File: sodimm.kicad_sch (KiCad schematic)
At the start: 3 parts, among them J1 PCB-Edge_SODIMM_144_SDR

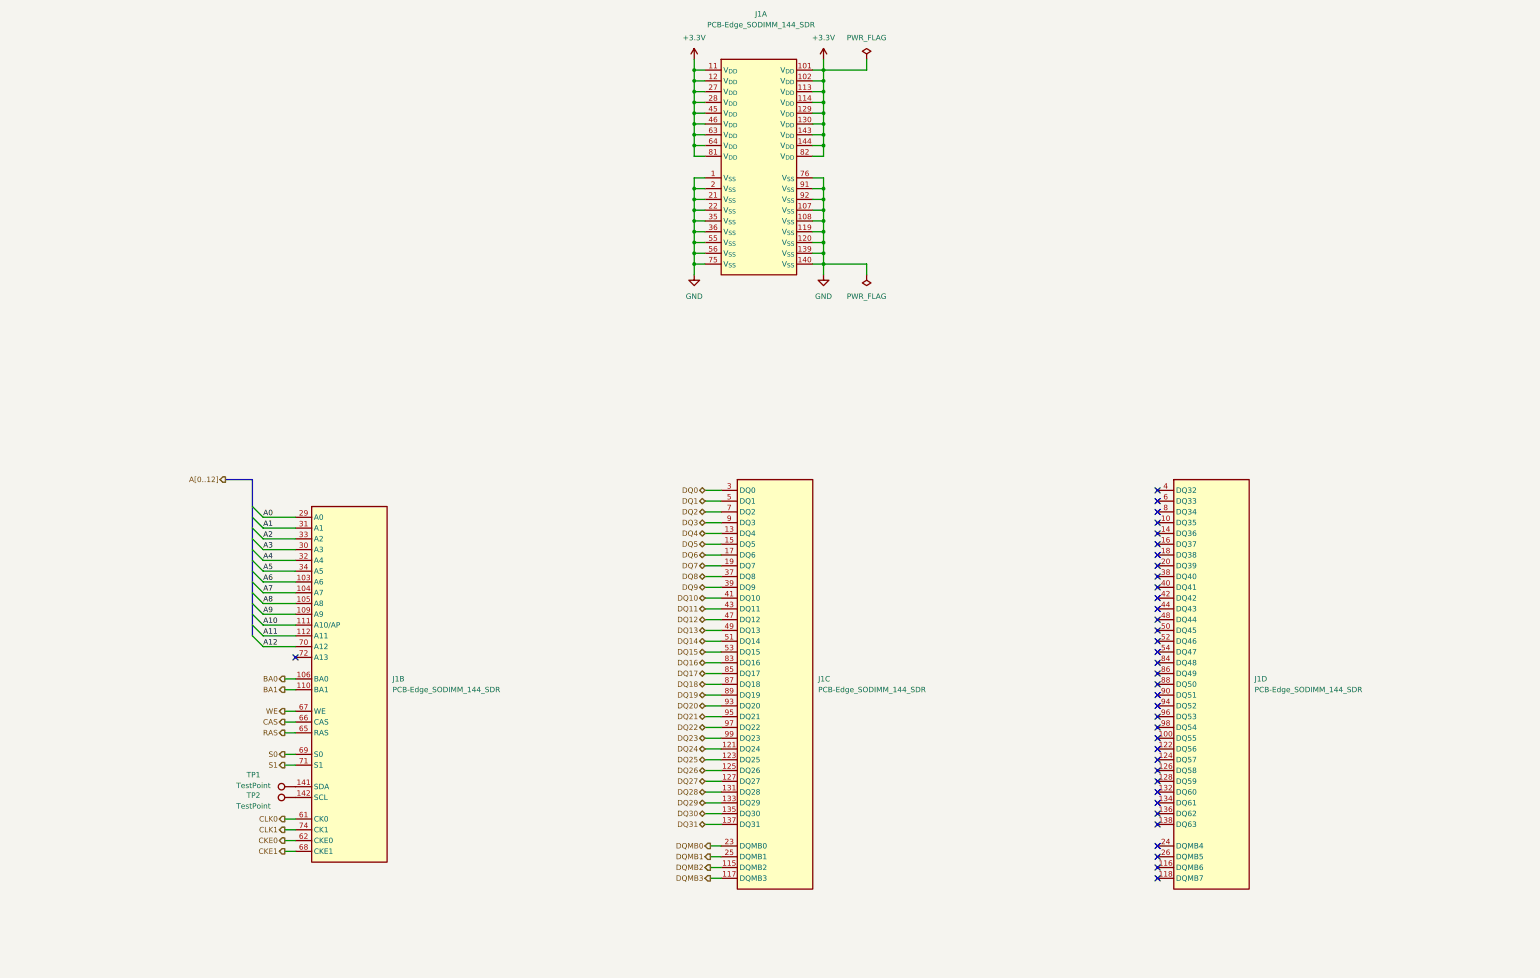
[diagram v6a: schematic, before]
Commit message: [#100470] Change schematic hierarchy
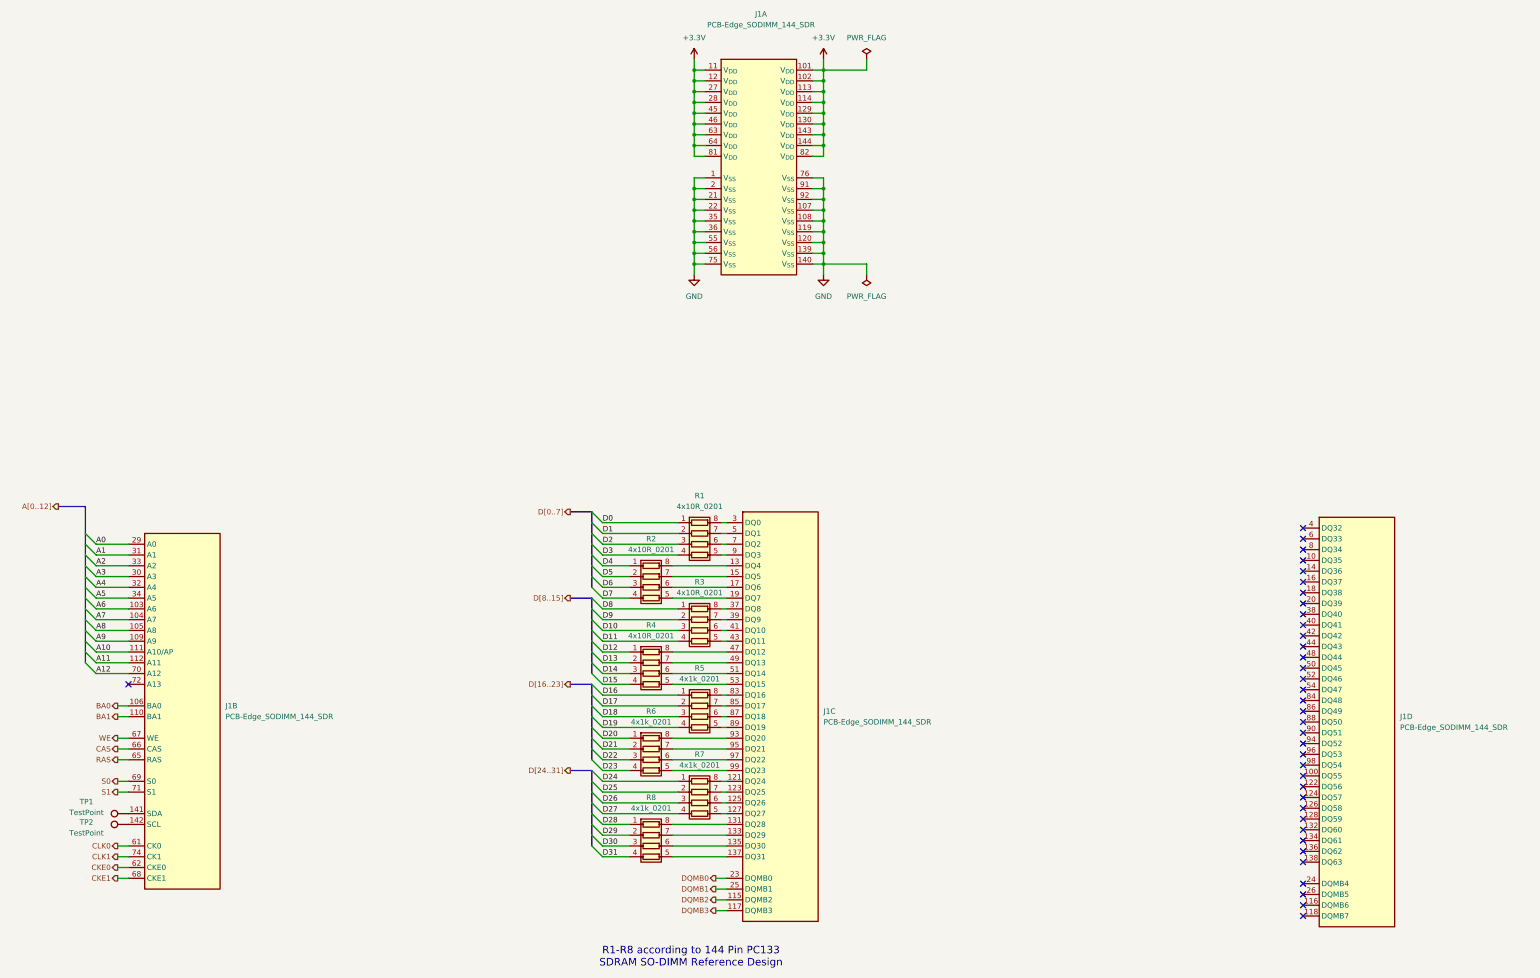
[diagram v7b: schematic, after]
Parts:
- added R1, R2, R3, R4: 4x10R_0201_array, antmicro-footprints:R_Array_4x0201_Panasonic_EXB18V, symbol antmicroResistorNetworksArrays:4x10R_0201_array
- added R5, R6, R7, R8: 4x1k_0201_array, antmicro-footprints:R_Array_4x0201_Panasonic_EXB18V, symbol antmicroResistorNetworksArrays:4x1k_0201_array
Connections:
- net DQ0: no longer names the net of J1.3 (DQ0)
- net DQ0: now also R1.8 (R1.2)
- net DQ1: no longer names the net of J1.5 (DQ1)
- net DQ1: now also R1.7 (R2.2)
- net DQ10: no longer names the net of J1.41 (DQ10)
- net DQ10: now also R3.6 (R3.2)
- net DQ11: no longer names the net of J1.43 (DQ11)
- net DQ11: now also R3.5 (R4.2)
- net DQ12: no longer names the net of J1.47 (DQ12)
- net DQ12: now also R4.8 (R1.2)
- net DQ13: no longer names the net of J1.49 (DQ13)
- net DQ13: now also R4.7 (R2.2)
- net DQ14: no longer names the net of J1.51 (DQ14)
- net DQ14: now also R4.6 (R3.2)
- net DQ15: no longer names the net of J1.53 (DQ15)
- net DQ15: now also R4.5 (R4.2)
- net DQ16: no longer names the net of J1.83 (DQ16)
- net DQ16: now also R5.8 (R1.2)
- net DQ17: no longer names the net of J1.85 (DQ17)
- net DQ17: now also R5.7 (R2.2)
- net DQ18: no longer names the net of J1.87 (DQ18)
- net DQ18: now also R5.6 (R3.2)
- net DQ19: no longer names the net of J1.89 (DQ19)
- net DQ19: now also R5.5 (R4.2)
- net DQ2: no longer names the net of J1.7 (DQ2)
- net DQ2: now also R1.6 (R3.2)
- net DQ20: no longer names the net of J1.93 (DQ20)
- net DQ20: now also R6.8 (R1.2)
- net DQ21: no longer names the net of J1.95 (DQ21)
- net DQ21: now also R6.7 (R2.2)
- net DQ22: no longer names the net of J1.97 (DQ22)
- net DQ22: now also R6.6 (R3.2)
- net DQ23: no longer names the net of J1.99 (DQ23)
- net DQ23: now also R6.5 (R4.2)
- net DQ24: no longer names the net of J1.121 (DQ24)
- net DQ24: now also R7.8 (R1.2)
- net DQ25: no longer names the net of J1.123 (DQ25)
- net DQ25: now also R7.7 (R2.2)
- net DQ26: no longer names the net of J1.125 (DQ26)
- net DQ26: now also R7.6 (R3.2)
- net DQ27: no longer names the net of J1.127 (DQ27)
- net DQ27: now also R7.5 (R4.2)
- net DQ28: no longer names the net of J1.131 (DQ28)
- net DQ28: now also R8.8 (R1.2)
- net DQ29: no longer names the net of J1.133 (DQ29)
- net DQ29: now also R8.7 (R2.2)
- net DQ3: no longer names the net of J1.9 (DQ3)
- net DQ3: now also R1.5 (R4.2)
- net DQ30: no longer names the net of J1.135 (DQ30)
- net DQ30: now also R8.6 (R3.2)
- net DQ31: no longer names the net of J1.137 (DQ31)
- net DQ31: now also R8.5 (R4.2)
- net DQ4: no longer names the net of J1.13 (DQ4)
- net DQ4: now also R2.8 (R1.2)
- net DQ5: no longer names the net of J1.15 (DQ5)
- net DQ5: now also R2.7 (R2.2)
- net DQ6: no longer names the net of J1.17 (DQ6)
- net DQ6: now also R2.6 (R3.2)
- net DQ7: no longer names the net of J1.19 (DQ7)
- net DQ7: now also R2.5 (R4.2)
- net DQ8: no longer names the net of J1.37 (DQ8)
- net DQ8: now also R3.8 (R1.2)
- net DQ9: no longer names the net of J1.39 (DQ9)
- net DQ9: now also R3.7 (R2.2)
- new net D0: R1.1 (R1.1)
- new net D1: R1.2 (R2.1)
- new net D10: R3.3 (R3.1)
- new net D11: R3.4 (R4.1)
- new net D12: R4.1 (R1.1)
- new net D13: R4.2 (R2.1)
- new net D14: R4.3 (R3.1)
- new net D15: R4.4 (R4.1)
- new net D16: R5.1 (R1.1)
- new net D17: R5.2 (R2.1)
- new net D18: R5.3 (R3.1)
- new net D19: R5.4 (R4.1)
- new net D2: R1.3 (R3.1)
- new net D20: R6.1 (R1.1)
- new net D21: R6.2 (R2.1)
- new net D22: R6.3 (R3.1)
- new net D23: R6.4 (R4.1)
- new net D24: R7.1 (R1.1)
- new net D25: R7.2 (R2.1)
- new net D26: R7.3 (R3.1)
- new net D27: R7.4 (R4.1)
- new net D28: R8.1 (R1.1)
- new net D29: R8.2 (R2.1)
- new net D3: R1.4 (R4.1)
- new net D30: R8.3 (R3.1)
- new net D31: R8.4 (R4.1)
- new net D4: R2.1 (R1.1)
- new net D5: R2.2 (R2.1)
- new net D6: R2.3 (R3.1)
- new net D7: R2.4 (R4.1)
- new net D8: R3.1 (R1.1)
- new net D9: R3.2 (R2.1)
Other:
- note added: "R1-R8 according to 144 Pin PC133 SDRAM SO-DIMM Reference Design"
- moved on the sheet: J1B, J1C, J1D, TP1, TP2
